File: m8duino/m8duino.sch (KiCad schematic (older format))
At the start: 8 parts, among them J1 Conn_02x03_Odd_Even, U1 ATMEGA8-16PU, Y1 Crystal

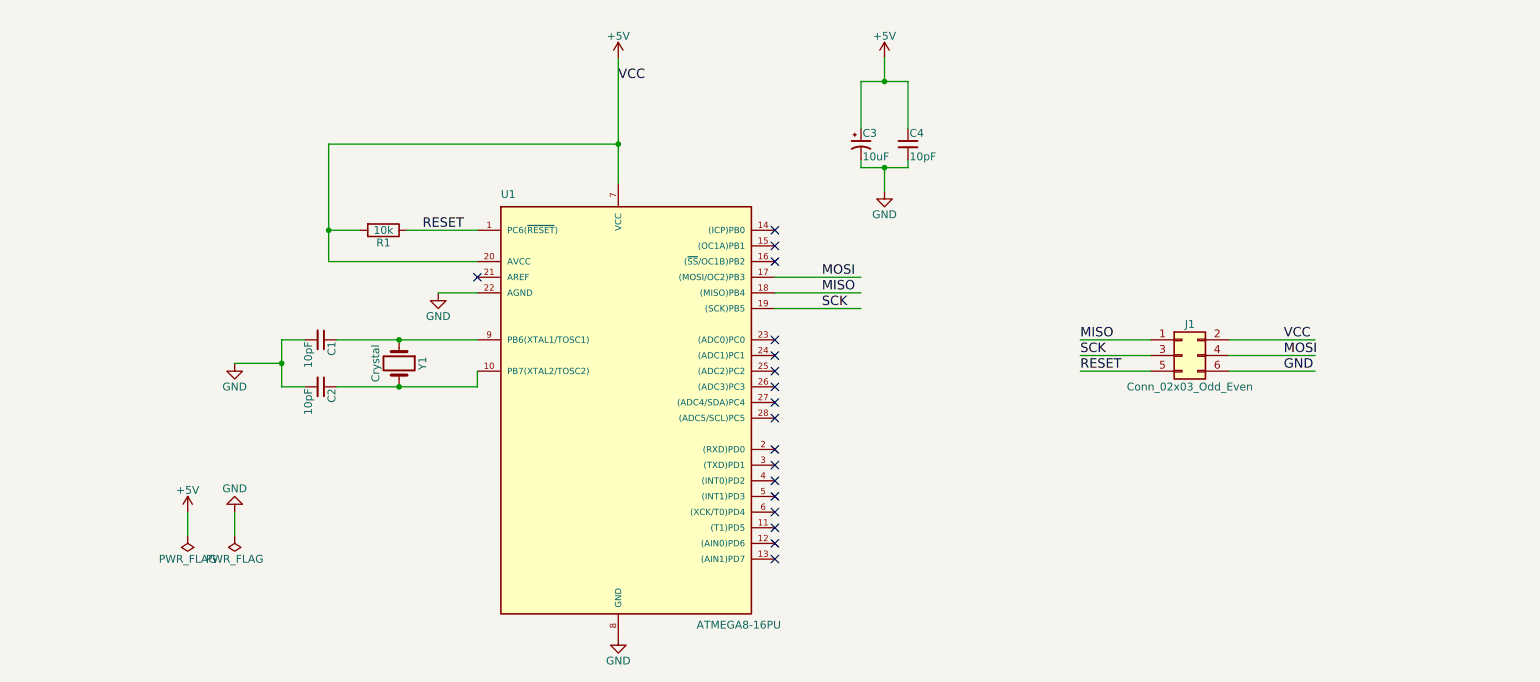
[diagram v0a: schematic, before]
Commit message: 完成测试板绘制;增加自动布线测试;
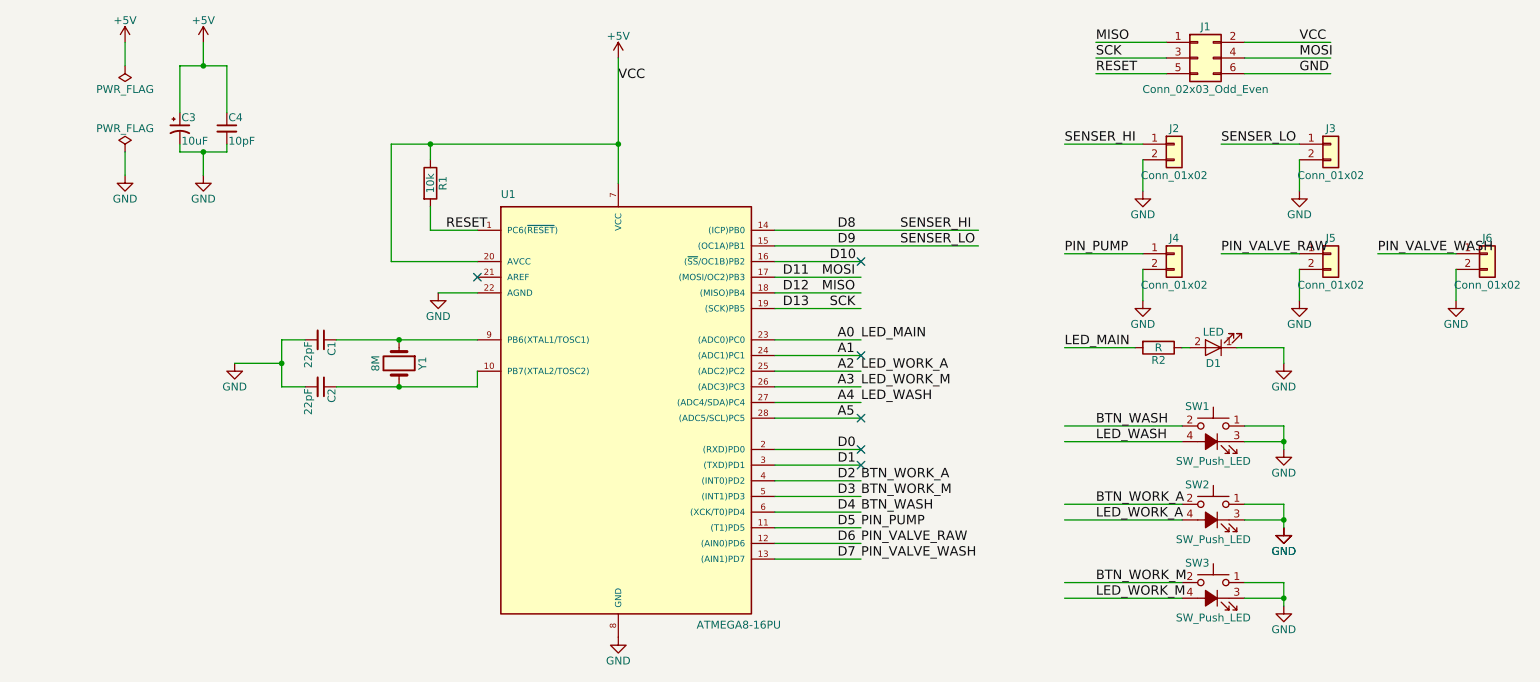
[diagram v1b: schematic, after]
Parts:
- added D1: LED, LEDs:LED_D4.0mm, symbol LED
- added J2, J3, J4, J5, J6: Conn_01x02, Connectors_Terminal_Blocks:TerminalBlock_Altech_AK300-2_P5.00mm, symbol Conn_01x02
- added R2: R, Resistors_THT:R_Axial_DIN0207_L6.3mm_D2.5mm_P10.16mm_Horizontal, symbol R
- added SW1, SW2, SW3: SW_Push_LED, Buttons_Switches_THT:Push_E-Switch_KS01Q01, symbol SW_Push_LED
- C1, C2: value 10pF -> 22pF; footprint (none) -> Capacitors_THT:C_Disc_D4.3mm_W1.9mm_P5.00mm
- C3: footprint (none) -> Capacitors_THT:CP_Radial_D5.0mm_P2.50mm
- C4: footprint (none) -> Capacitors_THT:C_Disc_D4.3mm_W1.9mm_P5.00mm
- J1: footprint (none) -> Pin_Headers:Pin_Header_Straight_2x03_Pitch2.54mm
- R1: footprint (none) -> Resistors_THT:R_Axial_DIN0309_L9.0mm_D3.2mm_P15.24mm_Horizontal
- U1: footprint DIL28 -> Housings_DIP:DIP-28_W7.62mm
- Y1: value Crystal -> 8M; footprint (none) -> Crystals:Crystal_HC18-U_Vertical
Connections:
- net labels added: A0, A1, A2, A3, A4, A5, BTN_WASH, BTN_WORK_A, BTN_WORK_M, D0, D1, D10, D11, D12, D13, D2, D3, D4, D5, D6, D7, D8, D9, LED_MAIN, LED_WASH, LED_WORK_A, LED_WORK_M, PIN_PUMP, PIN_VALVE_RAW, PIN_VALVE_WASH, SENSER_HI, SENSER_LO
- wire segments 33 -> 80
- no-connect marks 18 -> 6
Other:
- moved on the sheet: C3, C4, J1, R1

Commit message: 调整为 Arduino 系统开发板
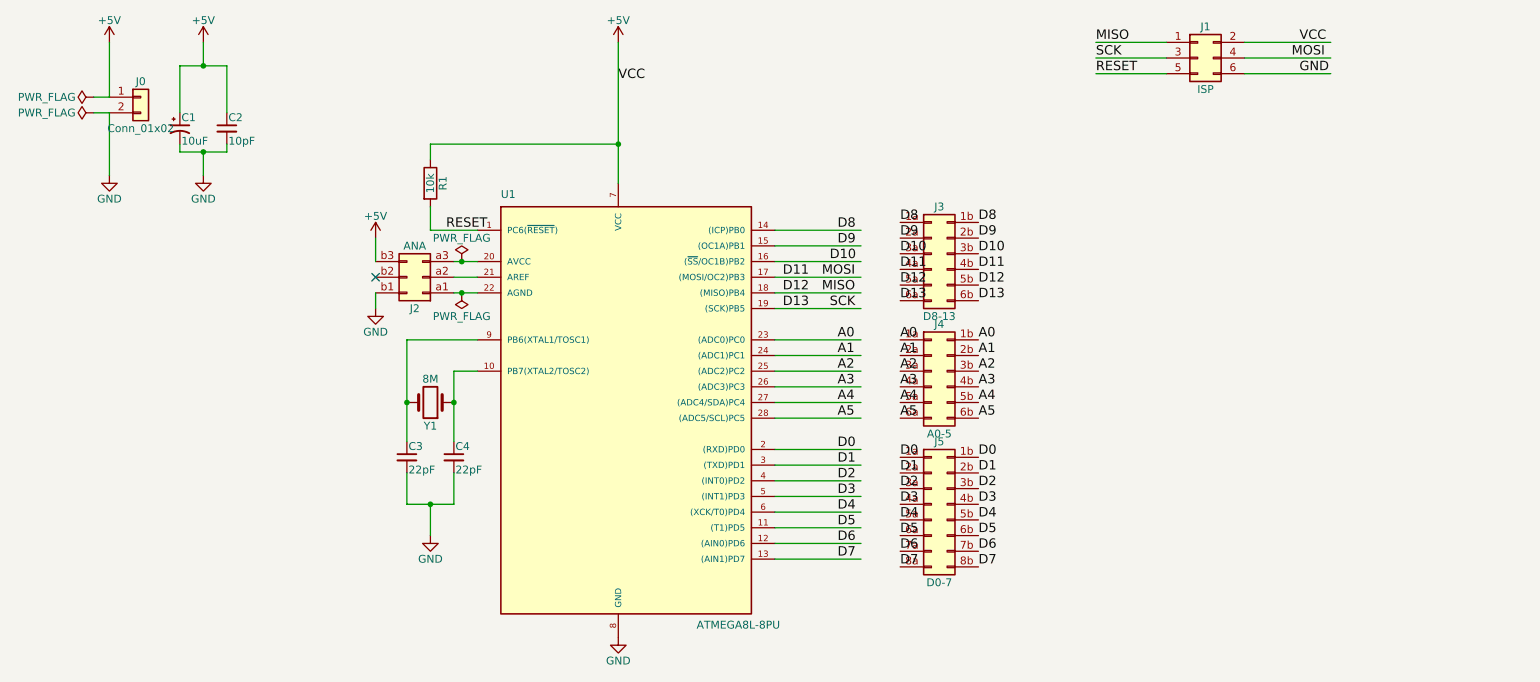
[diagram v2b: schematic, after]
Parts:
- removed D1: LED, LEDs:LED_D4.0mm, symbol LED
- removed J2, J3, J4, J5, J6: Conn_01x02, Connectors_Terminal_Blocks:TerminalBlock_Altech_AK300-2_P5.00mm, symbol Conn_01x02
- removed R2: R, Resistors_THT:R_Axial_DIN0207_L6.3mm_D2.5mm_P10.16mm_Horizontal, symbol R
- removed SW1, SW2, SW3: SW_Push_LED, Buttons_Switches_THT:Push_E-Switch_KS01Q01, symbol SW_Push_LED
- added J0: Conn_01x02, Pin_Headers:Pin_Header_Straight_1x02_Pitch2.54mm, symbol Conn_01x02
- added J2: ANA, Pin_Headers:Pin_Header_Straight_2x03_Pitch2.54mm, symbol Conn_02x03_Row_Letter_First
- added J3: D8-13, Pin_Headers:Pin_Header_Straight_2x06_Pitch2.54mm, symbol Conn_02x06_Row_Letter_Last
- added J4: A0-5, Pin_Headers:Pin_Header_Straight_2x06_Pitch2.54mm, symbol Conn_02x06_Row_Letter_Last
- added J5: D0-7, Pin_Headers:Pin_Header_Straight_2x08_Pitch2.54mm, symbol Conn_02x08_Row_Letter_Last
- J1: value Conn_02x03_Odd_Even -> ISP
- U1: value ATMEGA8-16PU -> ATMEGA8L-8PU
- Y1: footprint Crystals:Crystal_HC18-U_Vertical -> Crystals:Crystal_HC52-U_Vertical
- renumbered C3 to C1, C4 to C2, C1 to C3, C2 to C4
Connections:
- net labels removed: BTN_WASH, BTN_WORK_A, BTN_WORK_M, LED_MAIN, LED_WASH, LED_WORK_A, LED_WORK_M, PIN_PUMP, PIN_VALVE_RAW, PIN_VALVE_WASH, SENSER_HI, SENSER_LO
- wire segments 80 -> 56
- no-connect marks 6 -> 1
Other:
- moved on the sheet: C3, C4, Y1
